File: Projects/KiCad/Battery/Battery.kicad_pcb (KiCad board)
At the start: 2 copper layers, 110 x 95 mm, 15 parts, among them J1 Conn_01x02_Socket

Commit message: 原点を設定
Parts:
- moved BT1 174.7 mm to (189.8, 78.5)
- moved BT10 174.7 mm to (165.1, 49.8)
- moved BT2 174.7 mm to (159.8, 119.1)
- moved BT3 174.7 mm to (129.8, 78.5)
- moved BT4 174.7 mm to (99.8, 119.1)
- moved BT5 174.7 mm to (124.5, 63.8)
- moved BT6 174.7 mm to (165.1, 133.8)
- moved BT7 174.7 mm to (114.8, 119.1)
- moved BT8 174.7 mm to (144.8, 78.5)
- moved BT9 174.7 mm to (174.8, 119.1)
- moved J1 174.7 mm to (184.5, 125.8)
- moved REF** 174.7 mm to (174.8, 127.8)
- moved REF** 174.7 mm to (174.8, 67.8)
- moved REF** 174.7 mm to (114.8, 67.8)
- moved REF** 174.7 mm to (114.8, 127.8)

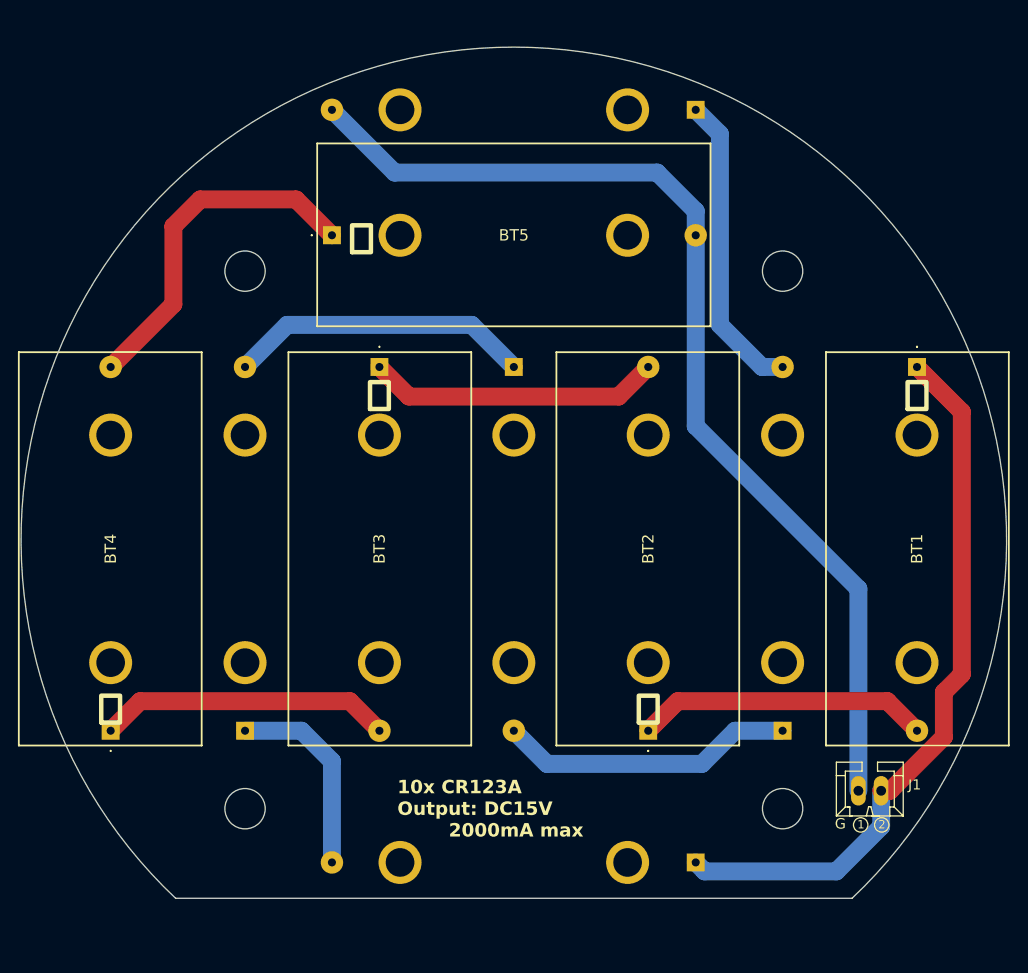
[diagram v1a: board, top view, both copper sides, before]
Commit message: バッテリーとケーブルグランドの干渉を解消
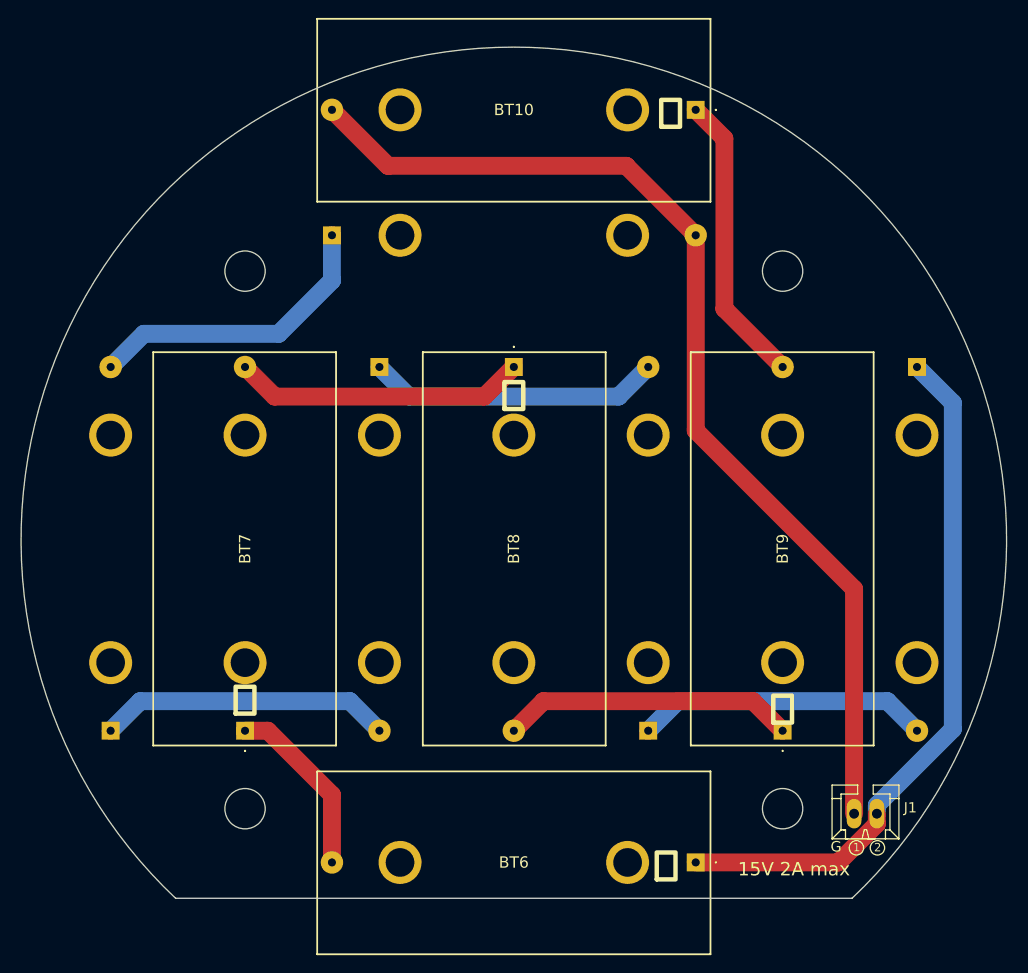
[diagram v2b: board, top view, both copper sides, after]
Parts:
- BT1, BT2, BT3, BT4, BT5: moved to B.Cu
- BT10, BT6, BT7, BT8, BT9: moved to F.Cu
- moved J1 2.60 mm to (184.0, 128.3)
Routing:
- net Net-(BT4--): track 39.2 -> 33.7 mm
- net Net-(BT1-+): track 80.9 -> 78.2 mm
- net Net-(BT6--): track 22.4 -> 20.2 mm
- net Net-(BT10-+): track 34.1 -> 32.7 mm
- net Net-(BT7--): track 33.9 -> 32.7 mm
- net Net-(BT10--): track 117.5 -> 118.3 mm
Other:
- board text added: "15V 2A max"
- board text removed: "10x CR123A Output: DC15V 2000mA max"
